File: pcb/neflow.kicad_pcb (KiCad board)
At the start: 2 copper layers, 53 parts, among them J101 1333870, J102 FAN0, J103 SSR0, J104 FAN1, J105 SSR1, J106 Temp0, J107 Temp1, Q101 Q_PMOS_GSD, Q102 IRLML2502, Q103 IRLML2502, Q104 IRLML2502, Q105 IRLML2502, Q106 IRLML2502, SW101 SW_Push, SW102 SW_Push, SW103 SW_Push, SW104 SW_Push, U101 Pico, U102 MAX31855KASA+T, U103 MAX31855KASA+T

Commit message: WIP: changes to pcb
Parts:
- added H1: MountingHole, MountingHole:MountingHole_3mm, F.Cu at (115.6, 130.1)
- added H2: MountingHole, MountingHole:MountingHole_3mm, F.Cu at (148.6, 130.1)
- added H3: MountingHole, MountingHole:MountingHole_3mm, F.Cu at (148.6, 180.1)
- added H4: MountingHole, MountingHole:MountingHole_3mm, F.Cu at (115.6, 180.1)
- J101, J106, J107: moved to B.Cu
- moved Brd101 202.6 mm to (-83.8, 81.3)
- moved J102 170.8 mm to (174.1, 89.8), turned to 90 degrees
- moved J104 168.8 mm to (174.0, 101.6), turned to 90 degrees
- moved PS101 163.1 mm to (129.6, 141.6), turned to 90 degrees
- moved J103 161.6 mm to (173.9, 78.1), turned to 90 degrees
- moved J101 160.8 mm to (124.8, 153.7), turned to -90 degrees
- moved J105 152.8 mm to (174.0, 68.3), turned to 90 degrees
- moved C104 142.8 mm to (137.1, 106.7), turned to -90 degrees
- moved JP101 134.7 mm to (145.3, 112.1), turned to -90 degrees
- moved C103 134.2 mm to (127.1, 106.7), turned to -90 degrees
- moved U103 133.3 mm to (128.3, 33.1)
- moved U102 128.4 mm to (128.3, 42.5)
- moved SW104 124.2 mm to (146.7, 34.5), turned to 180 degrees
- moved FB104 121.1 mm to (120.2, 30.6), turned to 90 degrees
- moved SW103 120.4 mm to (146.7, 43.2), turned to 180 degrees
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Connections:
- J106 pad 1: /T0- -> /T0+
- J106 pad 2: /T0+ -> /T0-
- J107 pad 1: /T1- -> /T1+
- J107 pad 2: /T1+ -> /T1-

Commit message: WIP: Finishing the pcb rev0
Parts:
- removed R107: 10K, Resistor_SMD:R_0603_1608Metric
- removed SW104: SW_Push, silicone_btn:BUTTON_SILICON
- added H5: MountingHole, MountingHole:MountingHole_3mm, F.Cu at (176.0, 45.7)
- added H6: MountingHole, MountingHole:MountingHole_3mm, F.Cu at (228.3, 45.7)
- added H7: MountingHole, MountingHole:MountingHole_3mm, F.Cu at (228.3, 220.2)
- added H8: MountingHole, MountingHole:MountingHole_3mm, F.Cu at (176.0, 220.2)
- J102, J103, J104, J105: moved to B.Cu
- moved Brd101 298.0 mm to (213.4, 58.9)
- moved D101 216.1 mm to (223.0, 113.3), turned to -90 degrees
- moved D102 214.6 mm to (223.0, 108.0), turned to 90 degrees
- moved R103 213.2 mm to (212.4, 125.1), turned to 180 degrees
- moved R101 212.7 mm to (218.4, 94.5), turned to 180 degrees
- moved C102 212.7 mm to (214.1, 51.1)
- moved R108 210.4 mm to (212.4, 123.1), turned to 180 degrees
- moved R104 210.1 mm to (212.4, 116.5), turned to 180 degrees
- moved R106 209.7 mm to (218.4, 85.6), turned to 180 degrees
- moved R102 209.6 mm to (218.2, 76.5), turned to 180 degrees
- moved C101 209.1 mm to (210.6, 51.1), turned to 180 degrees
- moved R105 206.7 mm to (212.3, 104.4), turned to 180 degrees
- moved R109 205.9 mm to (212.4, 110.4), turned to 180 degrees
- moved D103 203.2 mm to (213.4, 95.5)
- moved LS101 198.0 mm to (213.6, 90.4)
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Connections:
- net Net-(PS101-AC/L) renamed /AC/L
- net Net-(PS101-AC/N) renamed /AC/N
- U101 pad 11: MAX_SO -> unconnected-(U101-GPIO8-Pad11)
- U101 pad 13: unconnected-(U101-GND-Pad13) -> GND
- U101 pad 14: PI_TEMP0_~{CS} -> BTN0
- U101 pad 15: PI_TEMP1_~{CS} -> BTN1
- U101 pad 16: BTN0 -> BTN2
- U101 pad 17: BTN1 -> unconnected-(U101-GPIO13-Pad17)
- U101 pad 18: unconnected-(U101-GND-Pad18) -> GND
- U101 pad 19: BTN2 -> SCREEN_SDA
- U101 pad 20: BTN3 -> SCREEN_SCL
- U101 pad 21: SPK -> MAX_SPI_RX
- U101 pad 23: unconnected-(U101-GND-Pad23) -> GND
- U101 pad 24: SSR0 -> MAX_SPI_SCK
- U101 pad 25: SSR1 -> PI_TEMP0_~{CS}
- U101 pad 26: FAN0 -> PI_TEMP1_~{CS}
- U101 pad 27: FAN1 -> unconnected-(U101-GPIO21-Pad27)
- U101 pad 28: unconnected-(U101-GND-Pad28) -> GND
- U101 pad 3: unconnected-(U101-GND-Pad3) -> GND
- U101 pad 33: unconnected-(U101-AGND-Pad33) -> GND
- U101 pad 38: unconnected-(U101-GND-Pad38) -> GND
- U101 pad 4: SCREEN_SDA -> SSR0
- U101 pad 42: unconnected-(U101-GND-Pad42) -> GND
- U101 pad 5: SCREEN_SCL -> SSR1
- U101 pad 6: unconnected-(U101-GPIO4-Pad6) -> FAN0
- U101 pad 7: unconnected-(U101-GPIO5-Pad7) -> FAN1
- U101 pad 8: unconnected-(U101-GND-Pad8) -> GND
- U101 pad 9: MAX_SCK -> SPK
- U102 pad 5: MAX_SCK -> MAX_SPI_SCK
- U102 pad 7: MAX_SO -> MAX_SPI_RX
- U103 pad 5: MAX_SCK -> MAX_SPI_SCK
- U103 pad 7: MAX_SO -> MAX_SPI_RX
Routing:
- net GND: track 0.00 -> 379.1 mm, vias 0 -> 17
- net +3.3V: track 0.00 -> 179.4 mm, vias 0 -> 4
- net +5V: track 0.00 -> 116.9 mm
- net SCREEN_SDA: track 0.00 -> 40.2 mm
- net MAX_SPI_SCK: track 0.00 -> 36.5 mm
- net SCREEN_SCL: track 0.00 -> 34.7 mm
- net PI_TEMP1_~{CS}: track 0.00 -> 28.2 mm, vias 0 -> 2
- net BTN2: track 0.00 -> 24.2 mm, vias 0 -> 1
- net PI_TEMP0_~{CS}: track 0.00 -> 22.5 mm, vias 0 -> 1
- net BTN0: track 0.00 -> 21.9 mm, vias 0 -> 1
- net BTN1: track 0.00 -> 21.6 mm, vias 0 -> 1
- net MAX_SPI_RX: track 0.00 -> 20.9 mm
- net SPKB: track 0.00 -> 16.1 mm
- net SPK: track 0.00 -> 15.8 mm
- net SSR0: track 0.00 -> 15.5 mm
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- added copper zone on F.Cu, net /AC/L
- added copper zone on F.Cu, net /AC/N
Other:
- board outline added: 63.2 x 183.1 mm
- copper layers 2 -> 4

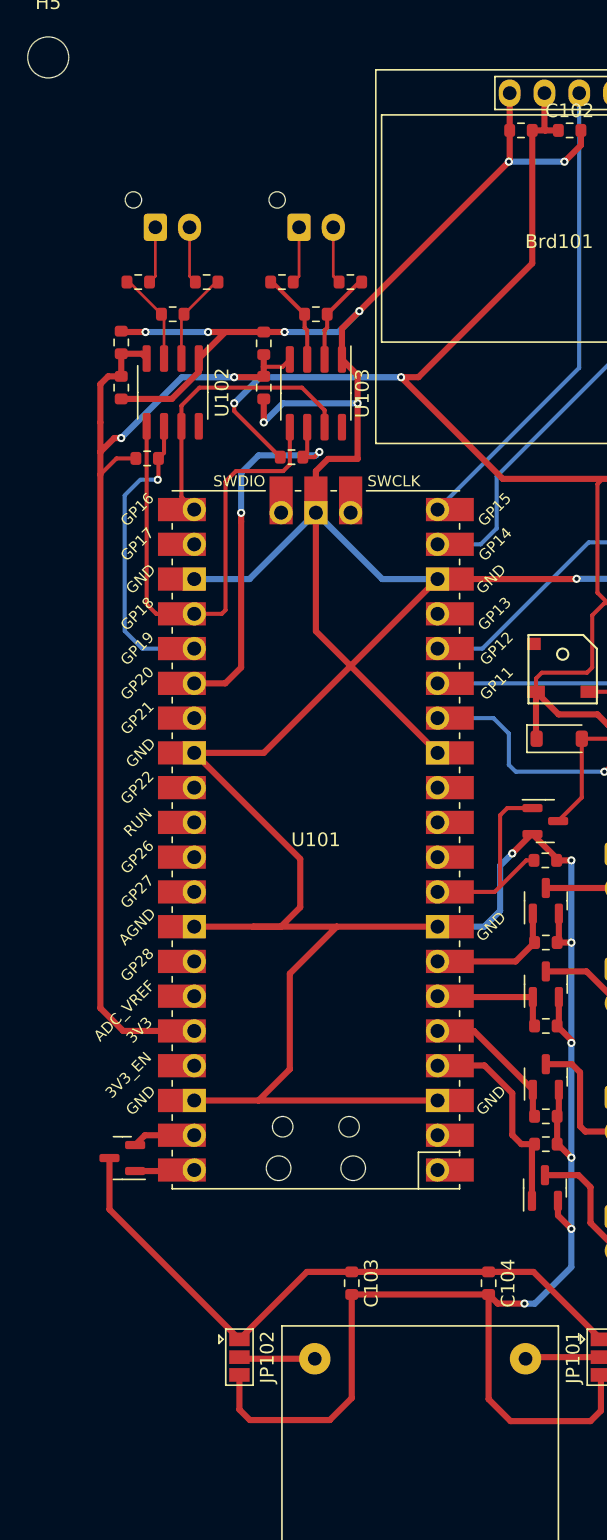
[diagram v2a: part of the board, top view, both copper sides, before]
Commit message: Added TLV803E supply voltage supervisor
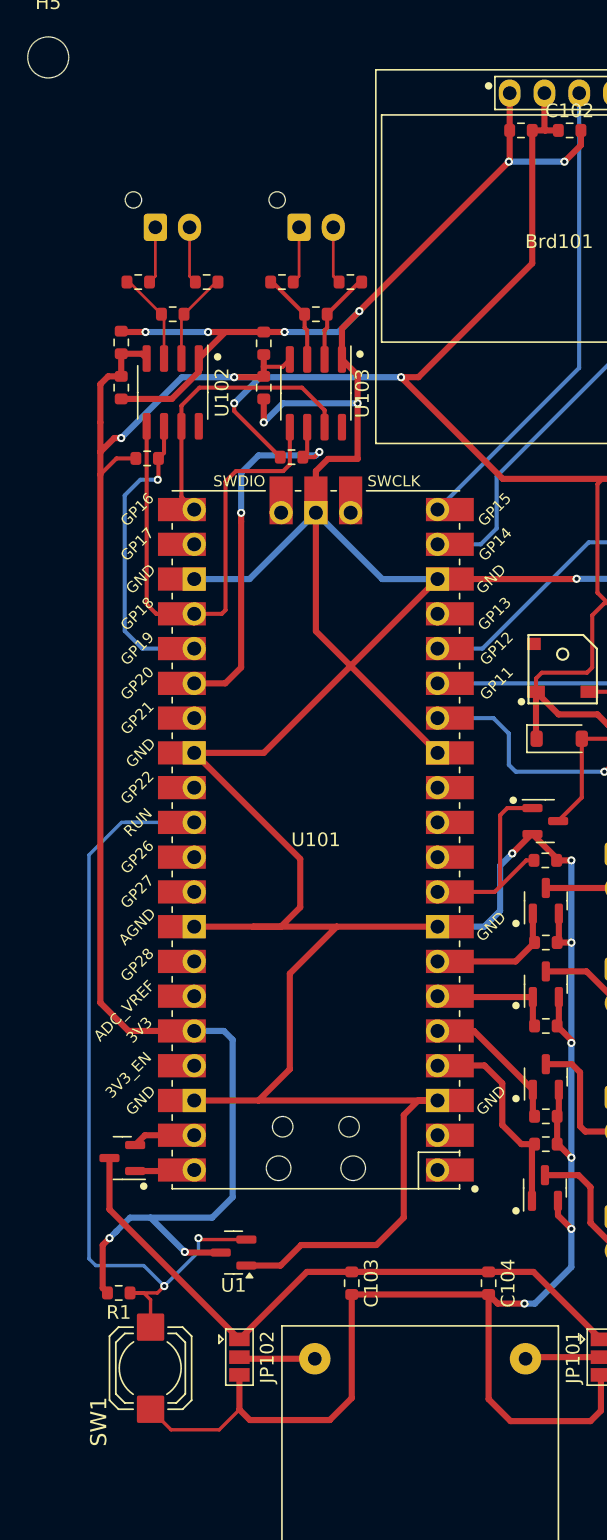
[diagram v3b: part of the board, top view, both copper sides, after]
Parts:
- added R1: 10K, Resistor_SMD:R_0603_1608Metric, F.Cu at (181.2, 136.0)
- added SW1: SW_Push, silicone_btn:BUTTON_SILICON, F.Cu at (183.5, 141.5)
- added U1: TLV803EF29DBZR, Package_TO_SOT_SMD:SOT-23, F.Cu at (189.6, 133.1)
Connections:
- U101 pad 30: unconnected-(U101-RUN-Pad30) -> RST
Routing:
- net RST: track 0.00 -> 60.4 mm, vias 0 -> 2
- net +3.3V: track 179.4 -> 214.6 mm, vias 4 -> 6
- net GND: track 379.1 -> 410.1 mm

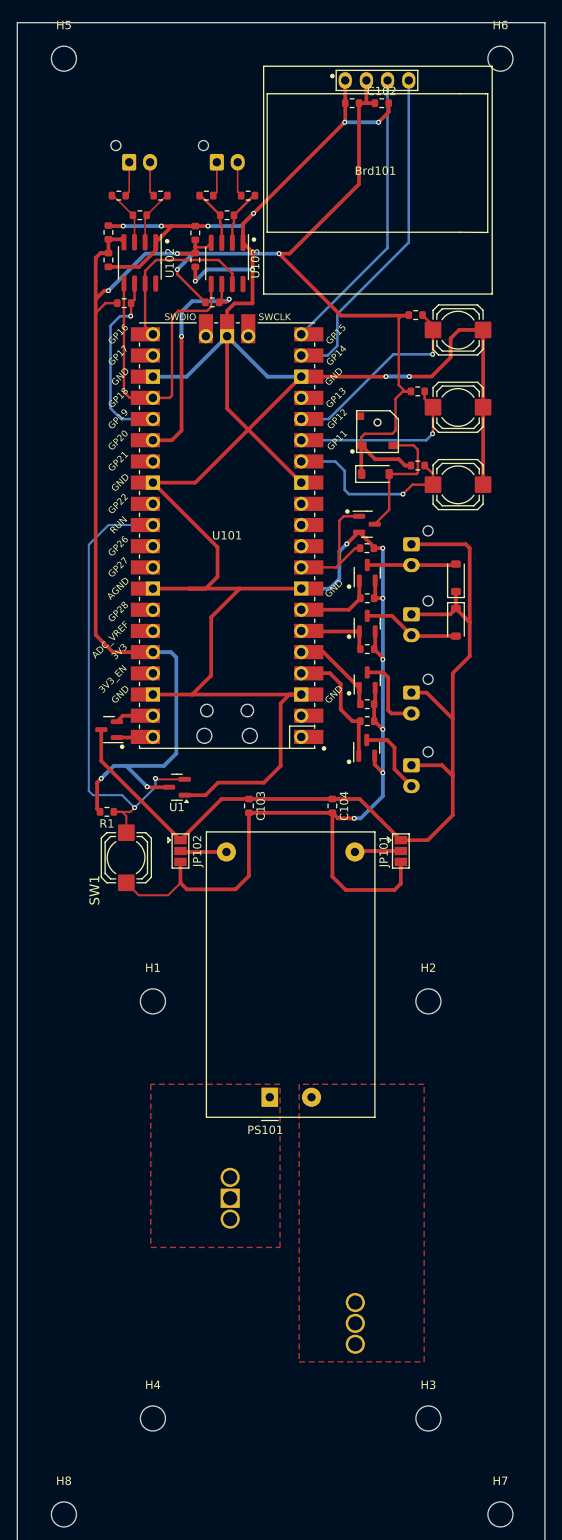
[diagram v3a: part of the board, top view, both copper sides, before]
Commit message: Adding new pcb changes for v2 pcb with reset logic
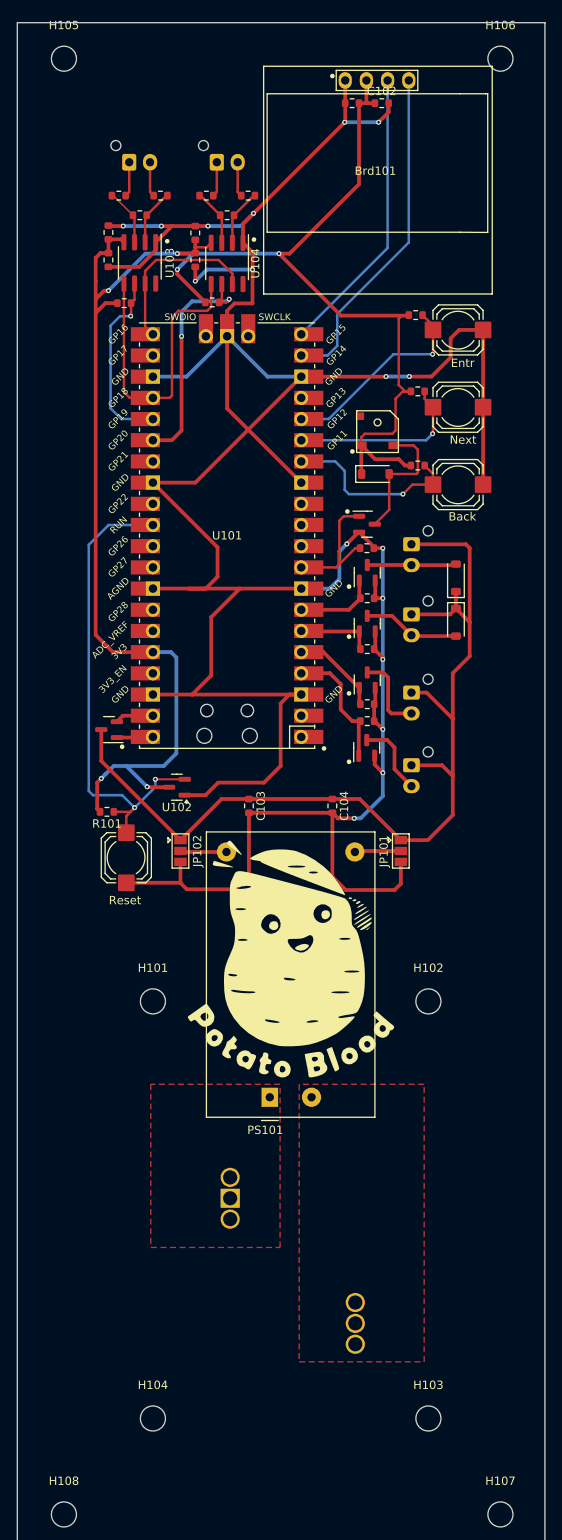
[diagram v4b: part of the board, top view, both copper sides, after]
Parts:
- added G***: LOGO, Branding:PT_BloodLogoSmall, F.Cu at (203.2, 153.6)
- renumbered D103 to D101, D101 to D102, D102 to D103, H1 to H101, H2 to H102, H3 to H103, H4 to H104, H5 to H105, H6 to H106, H7 to H107, H8 to H108, R1 to R101, R101 to R102, R102 to R103, R103 to R104, R104 to R105, R105 to R106, R106 to R107, SW1 to SW101, SW101 to SW102, SW102 to SW103, SW103 to SW104, U1 to U102, U102 to U103, U103 to U104
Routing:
- net GND: track 410.1 -> 408.9 mm
- net RST: track 60.4 -> 61.0 mm
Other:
- board text added: "Back"
- board text added: "Entr"
- board text added: "Next"
- board text added: "Reset"

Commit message: WIP: Stashing work to mess with vm
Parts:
- removed Brd101: SSD1306, SSD1306:128x64OLED
- removed C101, C102, C103, C104, C105, C106, C107, C108: 10uF, Resistor_SMD:R_0603_1608Metric
- removed C109, C110: 10nF, Resistor_SMD:R_0603_1608Metric
- removed D101, D102, D103: 1N4148W, Diode_SMD:D_SOD-123
- removed FB101, FB102, FB103, FB104: BLM18PG471, Resistor_SMD:R_0603_1608Metric
- removed H101, H102, H103, H104: MountingHole, MountingHole:MountingHole_3mm
- removed J101: 1333870, Unshareable:1333870
- removed J102: FAN0, Connector_JST:JST_XH_B2B-XH-AM_1x02_P2.50mm_Vertical
- removed J103: SSR0, Connector_JST:JST_XH_B2B-XH-AM_1x02_P2.50mm_Vertical
- removed J104: FAN1, Connector_JST:JST_XH_B2B-XH-AM_1x02_P2.50mm_Vertical
- removed J105: SSR1, Connector_JST:JST_XH_B2B-XH-AM_1x02_P2.50mm_Vertical
- removed J106: Temp0, Connector_JST:JST_XH_B2B-XH-AM_1x02_P2.50mm_Vertical
- removed J107: Temp1, Connector_JST:JST_XH_B2B-XH-AM_1x02_P2.50mm_Vertical
- removed JP101: VSel0, Jumper:SolderJumper-3_P1.3mm_Open_Pad1.0x1.5mm
- removed JP102: VSel1, Jumper:SolderJumper-3_P1.3mm_Open_Pad1.0x1.5mm
- removed LS101: Speaker, Library:PassiveBuzzerSMD_JiangsuHuaneng_MLT-5030
- removed PS101: HLK-PM01, Converter_ACDC:Converter_ACDC_HiLink_HLK-PMxx
- removed Q101: Q_PMOS_GSD, Package_TO_SOT_SMD:SOT-23
- removed Q102, Q103, Q104, Q105, Q106: IRLML2502, Package_TO_SOT_SMD:SOT-23
- removed R101, R102, R103, R104, R105, R106, R107, R108, R109, R110, R111: 10K, Resistor_SMD:R_0603_1608Metric
- removed SW101, SW102, SW103, SW104: SW_Push, silicone_btn:BUTTON_SILICON
- removed U101: Pico, MCU_RaspberryPi_and_Boards:RPi_Pico_SMD_TH
- removed U102: TLV803EF29DBZR, Package_TO_SOT_SMD:SOT-23
- removed U103, U104: MAX31855KASA+T, Package_SO:SOIC-8_3.9x4.9mm_P1.27mm
- added Brd601: SSD1306, SSD1306:128x64OLED, F.Cu at (201.7, 66.7)
- added C203: 10uF, Resistor_SMD:R_0603_1608Metric, F.Cu at (185.6, 132.9)
- added C204: 10uF, Resistor_SMD:R_0603_1608Metric, F.Cu at (194.2, 123.5)
- added C301: 4.7uF, Resistor_SMD:R_0603_1608Metric, F.Cu at (198.5, 99.0)
- added C302: 4.7uF, Resistor_SMD:R_0603_1608Metric, F.Cu at (194.8, 99.7)
- added C303: 4.7uF, Resistor_SMD:R_0603_1608Metric, F.Cu at (194.8, 98.2)
- added C304: 15pF, Resistor_SMD:R_0603_1608Metric, F.Cu at (190.8, 113.5)
- added C305: 15pF, Resistor_SMD:R_0603_1608Metric, F.Cu at (194.0, 113.6)
- added C306: 4.7uF, Resistor_SMD:R_0603_1608Metric, F.Cu at (198.5, 104.2)
- added C307: 100n, Resistor_SMD:R_0603_1608Metric, F.Cu at (186.8, 103.8)
- added C308: 100n, Resistor_SMD:R_0603_1608Metric, F.Cu at (194.1, 109.5)
- added C309: 100n, Resistor_SMD:R_0603_1608Metric, F.Cu at (190.8, 98.0)
- added C310: 100n, Resistor_SMD:R_0603_1608Metric, F.Cu at (190.8, 96.5)
- added C311: 100n, Resistor_SMD:R_0603_1608Metric, F.Cu at (187.6, 107.0)
- added C312: 100n, Resistor_SMD:R_0603_1608Metric, F.Cu at (197.4, 108.8)
- added C313: 100n, Resistor_SMD:R_0603_1608Metric, F.Cu at (186.8, 100.6)
- added C314: 100n, Resistor_SMD:R_0603_1608Metric, F.Cu at (200.1, 101.0)
- added C315: 100n, Resistor_SMD:R_0603_1608Metric, F.Cu at (197.8, 101.8)
- added C316: 100n, Resistor_SMD:R_0603_1608Metric, F.Cu at (186.8, 99.0)
- added C317: 100n, Resistor_SMD:R_0603_1608Metric, F.Cu at (190.0, 109.5)
- added C401: 100n, Resistor_SMD:R_0603_1608Metric, F.Cu at (186.8, 96.8)
- added C402: 100n, Resistor_SMD:R_0603_1608Metric, F.Cu at (184.7, 113.2)
- added C501: 10uF, Resistor_SMD:R_0603_1608Metric, F.Cu at (71.0, 81.0)
- added C502: 10uF, Resistor_SMD:R_0603_1608Metric, F.Cu at (71.0, 83.5)
- added C503: 10uF, Resistor_SMD:R_0603_1608Metric, F.Cu at (71.0, 86.0)
- added C504: 10uF, Resistor_SMD:R_0603_1608Metric, F.Cu at (71.0, 88.6)
- added C505: 10nF, Resistor_SMD:R_0603_1608Metric, F.Cu at (71.0, 91.1)
- added C506: 10nF, Resistor_SMD:R_0603_1608Metric, F.Cu at (71.0, 93.6)
- added C601: 10uF, Resistor_SMD:R_0603_1608Metric, F.Cu at (145.1, 155.1)
- added C602: 10uF, Resistor_SMD:R_0603_1608Metric, F.Cu at (99.0, 113.8)
- added C701: 10uF, Resistor_SMD:R_0603_1608Metric, F.Cu at (25.3, 111.8)
- added D301: PWR_LED, LED_SMD:LED_0805_2012Metric, F.Cu at (53.7, 125.6)
- added D501: 1N4148W, Diode_SMD:D_SOD-123, F.Cu at (76.8, 62.9)
- added D502: 1N4148W, Diode_SMD:D_SOD-123, F.Cu at (76.8, 66.3)
- added D601: 1N4148W, Diode_SMD:D_SOD-123, F.Cu at (97.1, 133.1)
- added FB501: BLM18PG471, Resistor_SMD:R_0603_1608Metric, F.Cu at (75.0, 81.0)
- added FB502: BLM18PG471, Resistor_SMD:R_0603_1608Metric, F.Cu at (75.0, 83.5)
- added FB503: BLM18PG471, Resistor_SMD:R_0603_1608Metric, F.Cu at (75.0, 86.0)
- added FB504: BLM18PG471, Resistor_SMD:R_0603_1608Metric, F.Cu at (75.0, 88.6)
- added H201: MountingHole, MountingHole:MountingHole_3mm, F.Cu at (115.8, 263.4)
- added H202: MountingHole, MountingHole:MountingHole_3mm, F.Cu at (92.6, 258.2)
- added H203: MountingHole, MountingHole:MountingHole_3mm, F.Cu at (63.4, 247.8)
- added H204: MountingHole, MountingHole:MountingHole_3mm, F.Cu at (125.0, 233.6)
- added J201: 1333870, Library:1333870, B.Cu at (195.9, 182.3)
- added J302: Debug Socket, Connector_JST:JST_XH_B3B-XH-AM_1x03_P2.50mm_Vertical, F.Cu at (30.1, 147.9)
- added J501: Temp0, Connector_JST:JST_XH_B2B-XH-AM_1x02_P2.50mm_Vertical, F.Cu at (63.0, 64.6)
- added J502: Temp1, Connector_JST:JST_XH_B2B-XH-AM_1x02_P2.50mm_Vertical, F.Cu at (63.0, 72.4)
- added J503: SSR0, Connector_JST:JST_XH_B2B-XH-AM_1x02_P2.50mm_Vertical, F.Cu at (63.0, 80.2)
- added J504: SSR1, Connector_JST:JST_XH_B2B-XH-AM_1x02_P2.50mm_Vertical, F.Cu at (63.0, 88.0)
- added J505: FAN0, Connector_JST:JST_XH_B2B-XH-AM_1x02_P2.50mm_Vertical, F.Cu at (63.0, 95.8)
- added J506: FAN1, Connector_JST:JST_XH_B2B-XH-AM_1x02_P2.50mm_Vertical, F.Cu at (63.0, 103.6)
- added J701: Micro_SD_Card_Det2, Connector_Card:microSD_HC_Hirose_DM3AT-SF-PEJM5, F.Cu at (92.6, 170.3)
- added JP201: VSel0, Jumper:SolderJumper-3_P1.3mm_Open_Pad1.0x1.5mm, F.Cu at (216.4, 140.7)
- added JP202: VSel1, Jumper:SolderJumper-3_P1.3mm_Open_Pad1.0x1.5mm, F.Cu at (190.0, 140.7)
- added L302: 3.3uH, SparkFun-Coil:0806_Polarized, F.Cu at (194.9, 96.4)
- added LS601: Speaker, Library:PassiveBuzzerSMD_JiangsuHuaneng_MLT-5030, F.Cu at (91.1, 134.5)
- added PS201: HLK-PM01, ACDCLibrary:Converter_ACDC_HiLink_HLK-PMxx, F.Cu at (200.7, 170.2)
- added Q501: IRLML2502, Package_TO_SOT_SMD:SOT-23, F.Cu at (71.4, 63.7)
- added Q502: IRLML2502, Package_TO_SOT_SMD:SOT-23, F.Cu at (71.4, 68.3)
- added Q503: IRLML2502, Package_TO_SOT_SMD:SOT-23, F.Cu at (71.4, 72.9)
- added Q504: IRLML2502, Package_TO_SOT_SMD:SOT-23, F.Cu at (71.4, 77.5)
- added Q601: IRLML2502, Package_TO_SOT_SMD:SOT-23, F.Cu at (99.1, 145.0)
- added R201: 10K, Resistor_SMD:R_0603_1608Metric, F.Cu at (248.3, 127.0)
- added R301: 33R, Resistor_SMD:R_0603_1608Metric, F.Cu at (197.8, 96.7)
- added R302: 1k, Resistor_SMD:R_0603_1608Metric, F.Cu at (192.9, 111.7)
- added R303: 4.7k, Resistor_SMD:R_0603_1608Metric, F.Cu at (45.5, 136.4)
- added R401: 10k, Resistor_SMD:R_0603_1608Metric, F.Cu at (186.0, 90.4)
- added R402: 10k, Resistor_SMD:R_0603_1608Metric, F.Cu at (186.0, 106.1)
- added R501: 10K, Resistor_SMD:R_0603_1608Metric, F.Cu at (75.0, 91.1)
- added R502: 10K, Resistor_SMD:R_0603_1608Metric, F.Cu at (75.0, 93.6)
- added R503: 10K, Resistor_SMD:R_0603_1608Metric, F.Cu at (79.0, 81.0)
- added R504: 10K, Resistor_SMD:R_0603_1608Metric, F.Cu at (79.0, 83.5)
- added R505: 10K, Resistor_SMD:R_0603_1608Metric, F.Cu at (79.0, 86.0)
- added R507: 10K, Resistor_SMD:R_0603_1608Metric, F.Cu at (79.0, 88.6)
- added R601: 10K, Resistor_SMD:R_0603_1608Metric, F.Cu at (99.0, 116.3)
- added R602: 10K, Resistor_SMD:R_0603_1608Metric, F.Cu at (99.0, 118.9)
- added R603: 10K, Resistor_SMD:R_0603_1608Metric, F.Cu at (99.0, 121.4)
- added R604: 10K, Resistor_SMD:R_0603_1608Metric, F.Cu at (99.0, 123.9)
- added R701: 10K, Resistor_SMD:R_0603_1608Metric, F.Cu at (20.2, 117.9)
- added R702: 10K, Resistor_SMD:R_0603_1608Metric, F.Cu at (20.0, 124.2)
- added R703: 10K, Resistor_SMD:R_0603_1608Metric, F.Cu at (21.6, 133.4)
- added SW201: SW_Push, silicone_btn:BUTTON_SILICON, F.Cu at (251.3, 141.1)
- added SW601: SW_Push, silicone_btn:BUTTON_SILICON, F.Cu at (211.8, 87.0)
- added SW602: SW_Push, silicone_btn:BUTTON_SILICON, F.Cu at (201.8, 87.0)
- added SW603: SW_Push, silicone_btn:BUTTON_SILICON, F.Cu at (191.8, 87.0)
- added U201: RT9080-33GJ5, Package_TO_SOT_SMD:TSOT-23-5, F.Cu at (193.2, 133.0)
- added U202: TLV803EF29DBZR, Package_TO_SOT_SMD:SOT-23, F.Cu at (240.7, 122.4)
- added U301: RP2350A-QFN60, Package_DFN_QFN:QFN-60-1EP_7x7mm_P0.4mm_EP3.4x3.4mm_ThermalVias, F.Cu at (192.5, 104.5)
- added U401: W25Q128JVS, Package_SO:SOIC-8_5.23x5.23mm_P1.27mm, F.Cu at (181.8, 93.2)
- added U402: ~, Package_SO:SOIC-8_3.9x4.9mm_P1.27mm, F.Cu at (182.0, 108.6)
- added U501: MAX31855KASA+T, Package_SO:SOIC-8_3.9x4.9mm_P1.27mm, F.Cu at (208.9, 100.5)
- added U502: MAX31855KASA+T, Package_SO:SOIC-8_3.9x4.9mm_P1.27mm, F.Cu at (153.3, 103.0)
- added Y301: ABM8-272-T3, SparkFun-Clock:Crystal_SMD_3.2x2.5mm, F.Cu at (192.7, 116.0)
- moved G*** 73.5 mm to (276.0, 164.0)
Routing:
- net GND: track 408.9 -> 8.38 mm, vias 17 -> 4
- net +3.3V: track 214.6 -> 16.0 mm, vias 6 -> 0
- net +5V: track 116.9 -> 0.00 mm
- net RST: track 61.0 -> 0.00 mm, vias 2 -> 0
- net SCREEN_SDA: track 40.2 -> 0.00 mm
- net MAX_SPI_SCK: track 36.5 -> 0.00 mm
- net SCREEN_SCL: track 34.7 -> 0.00 mm
- net PI_TEMP1_~{CS}: track 28.2 -> 0.00 mm, vias 2 -> 0
- net BTN2: track 24.2 -> 0.00 mm, vias 1 -> 0
- net PI_TEMP0_~{CS}: track 22.5 -> 0.00 mm, vias 1 -> 0
- net BTN0: track 21.9 -> 0.00 mm, vias 1 -> 0
- net BTN1: track 21.6 -> 0.00 mm, vias 1 -> 0
- net MAX_SPI_RX: track 20.9 -> 0.00 mm
- net +1.1V: track 0.00 -> 20.3 mm, vias 0 -> 8
- net SPKB: track 16.1 -> 0.00 mm
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- added copper zone on F.Cu, net (none)
- added copper zone on F.Cu, net +1.1V
- added copper zone on F.Cu, net +3.3V
- added copper zone on F.Cu, net /RP2350 Core/VREG_LX
- added copper zone on F.Cu, net GND
- removed copper zone on F.Cu, net /AC/L
- removed copper zone on F.Cu, net /AC/N
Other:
- board text removed: "Back"
- board text removed: "Entr"
- board text removed: "Next"
- board text removed: "Reset"
